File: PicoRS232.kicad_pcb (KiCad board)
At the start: 2 copper layers, 78.7 x 72.9 mm, 25 parts, among them J1 RS232_0, J2 RS232_1, J3 RS232_2, J4 RS232_3, J5 RS232_4, J6 RS232_5, U1 MAX3232CDR, U2 MAX3232CDR, U3 MAX3232CDR

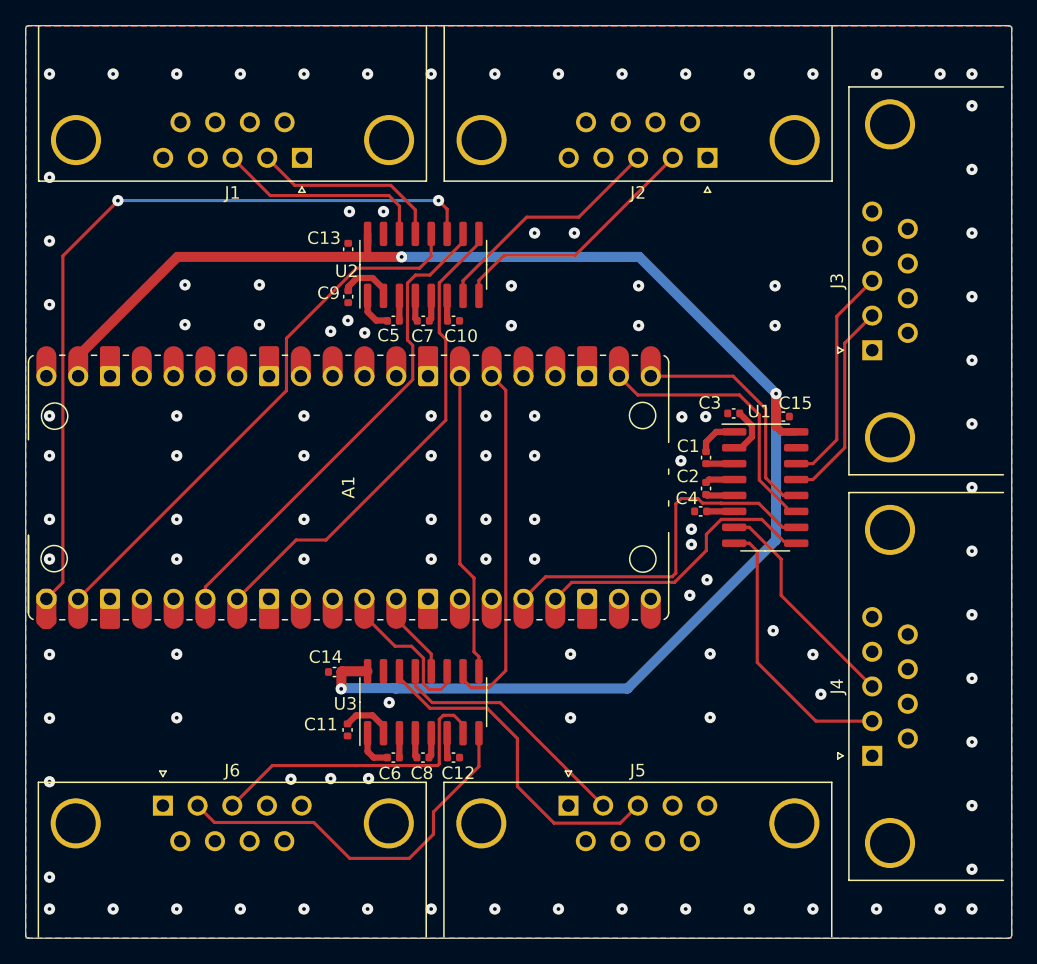
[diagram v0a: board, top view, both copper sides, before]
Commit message: Break out unused GPIO pins to headers.
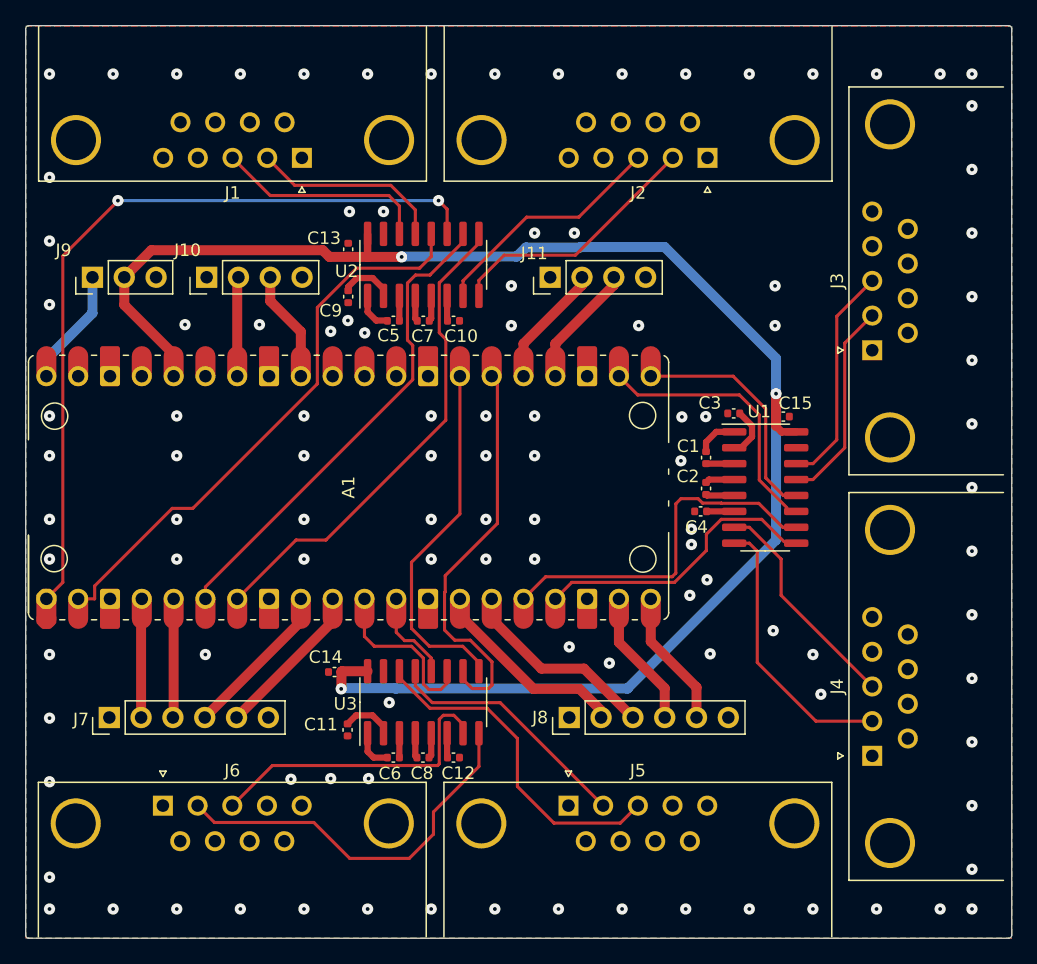
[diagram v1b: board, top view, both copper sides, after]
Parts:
- added J10: Conn_01x04_Male, Connector_PinHeader_2.54mm:PinHeader_1x04_P2.54mm_Vertical, F.Cu at (60.5, 54.5)
- added J11: Conn_01x04_Male, Connector_PinHeader_2.54mm:PinHeader_1x04_P2.54mm_Vertical, F.Cu at (87.9, 54.5)
- added J7: Conn_01x06_Male, Connector_PinHeader_2.54mm:PinHeader_1x06_P2.54mm_Vertical, F.Cu at (52.7, 89.6)
- added J8: Conn_01x06_Male, Connector_PinHeader_2.54mm:PinHeader_1x06_P2.54mm_Vertical, F.Cu at (89.4, 89.6)
- added J9: Conn_01x03_Male, Connector_PinHeader_2.54mm:PinHeader_1x03_P2.54mm_Vertical, F.Cu at (51.3, 54.5)
- J2: value RS232_1 -> RS232_0
- J3: value RS232_2 -> RS232_0
- J4: value RS232_3 -> RS232_0
- J5: value RS232_4 -> RS232_0
- J6: value RS232_5 -> RS232_0
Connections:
- A1 pad 10: unconnected-(A1-Pad10) -> GPIO7
- A1 pad 14: unconnected-(A1-Pad14) -> GPIO10
- A1 pad 15: unconnected-(A1-Pad15) -> GPIO11
- A1 pad 19: unconnected-(A1-Pad19) -> GPIO14
- A1 pad 20: unconnected-(A1-Pad20) -> GPIO15
- A1 pad 24: unconnected-(A1-Pad24) -> GPIO18
- A1 pad 25: unconnected-(A1-Pad25) -> GPIO19
- A1 pad 32: unconnected-(A1-Pad32) -> GPIO27
- A1 pad 34: unconnected-(A1-Pad34) -> GPIO28
- A1 pad 36: unconnected-(A1-Pad36) -> +3V3
- A1 pad 39: +3V3 -> unconnected-(A1-Pad39)
- A1 pad 4: unconnected-(A1-Pad4) -> GPIO2
- A1 pad 5: unconnected-(A1-Pad5) -> GPIO3
- A1 pad 9: unconnected-(A1-Pad9) -> GPIO6
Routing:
- net GPIO10: track 0.00 -> 14.6 mm
- net GPIO11: track 0.00 -> 14.5 mm
- net GPIO6: track 0.00 -> 10.9 mm
- net GPIO7: track 0.00 -> 10.9 mm
- net +5V: track 0.00 -> 9.42 mm
- net GPIO2: track 0.00 -> 9.42 mm
- net GPIO14: track 0.00 -> 9.39 mm
- net GPIO15: track 0.00 -> 9.39 mm
- net GPIO27: track 0.00 -> 8.91 mm
- net GPIO19: track 0.00 -> 8.23 mm
- net GPIO18: track 0.00 -> 8.23 mm
- net GPIO3: track 0.00 -> 7.82 mm
- net GPIO28: track 0.00 -> 7.80 mm
- net +3V3: track 124.6 -> 128.8 mm
- net UART5_RX: track 24.2 -> 28.3 mm
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
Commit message: Organize schematic and add mounting holes.
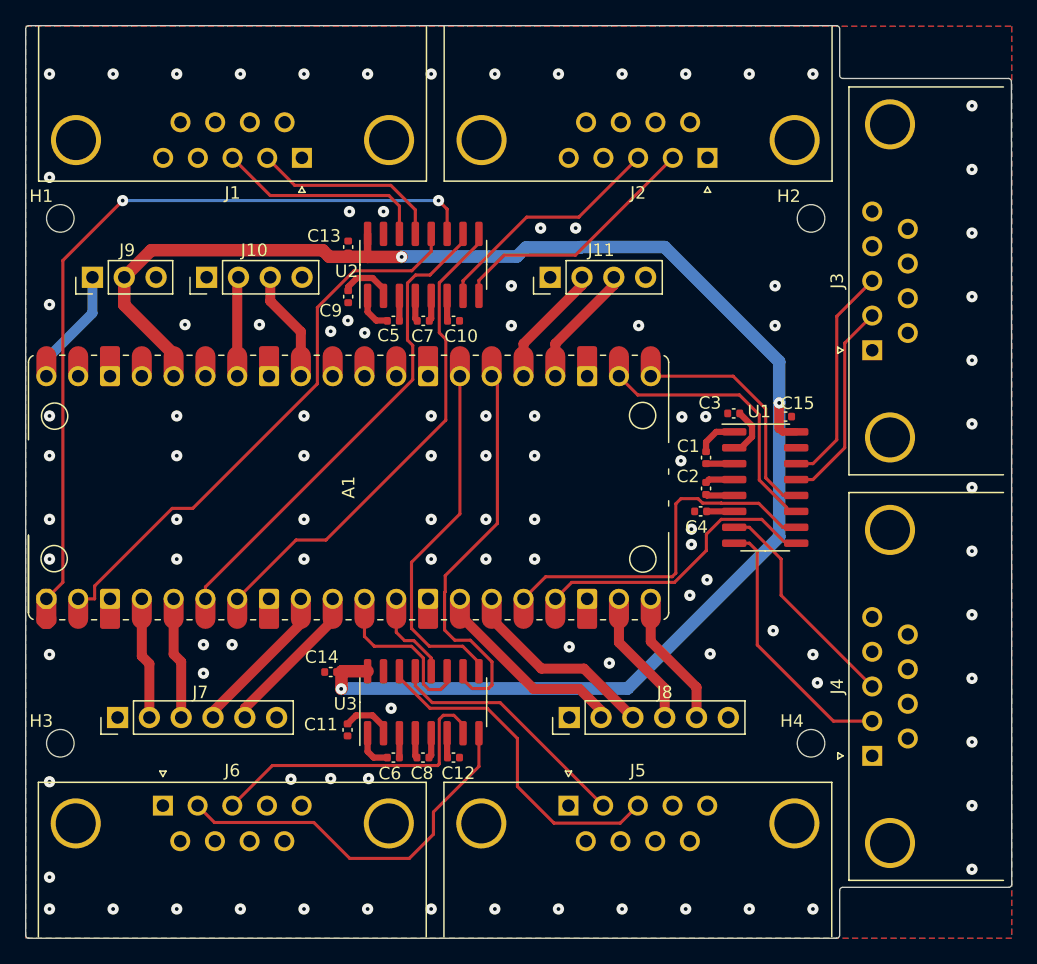
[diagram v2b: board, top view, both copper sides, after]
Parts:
- added H1: MountingHole_2.2mm_M2, MountingHole:MountingHole_2.2mm_M2, F.Cu at (48.8, 49.8)
- added H2: MountingHole_2.2mm_M2, MountingHole:MountingHole_2.2mm_M2, F.Cu at (108.7, 49.8)
- added H3: MountingHole_2.2mm_M2, MountingHole:MountingHole_2.2mm_M2, F.Cu at (48.8, 91.7)
- added H4: MountingHole_2.2mm_M2, MountingHole:MountingHole_2.2mm_M2, F.Cu at (108.7, 91.7)
- moved J7 0.66 mm to (53.3, 89.6)
- moved C14 0.30 mm to (70.4, 86.0)
- moved C15 0.18 mm to (106.7, 65.6)
- moved C13 0.18 mm to (71.8, 52.1)
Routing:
- net GPIO2: track 9.42 -> 8.13 mm
- net RS232_3_RX: track 22.1 -> 21.3 mm
- net +3V3: track 128.8 -> 128.1 mm
- net GND: vias 108 -> 102
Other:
- outline, holes or cut-outs redrawn

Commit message: Silkscreen and cosmetic improvements to PCB.
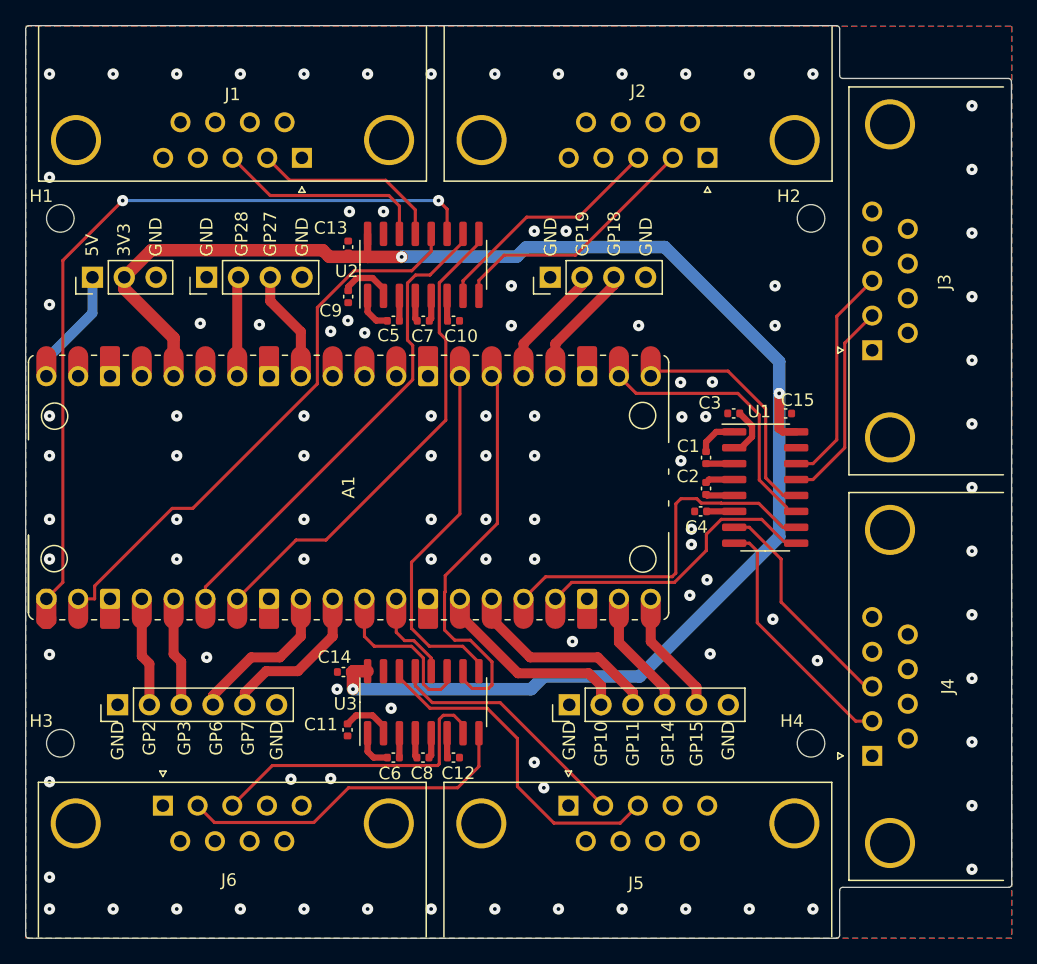
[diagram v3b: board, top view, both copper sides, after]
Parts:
- moved J7 1.02 mm to (53.3, 88.6)
- moved J8 1.02 mm to (89.4, 88.6)
- moved C14 1.02 mm to (71.4, 86.0)
- moved C15 0.25 mm to (106.7, 65.4)
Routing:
- net RS232_5_RX: track 30.9 -> 27.5 mm
- net +3V3: track 128.1 -> 127.1 mm
- net RS232_3_RX: track 21.3 -> 20.3 mm
- net GPIO3: track 8.13 -> 7.11 mm
- net GPIO2: track 8.13 -> 7.11 mm
- net GPIO15: track 9.39 -> 8.37 mm
- net GPIO14: track 9.39 -> 8.37 mm
- net GPIO10: track 14.6 -> 15.2 mm
- net GPIO11: track 14.5 -> 14.0 mm
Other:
- board text added: "3V3"
- board text added: "5V"
- board text added: "GND"
- board text added: "GP10"
- board text added: "GP11"
- board text added: "GP14"
- board text added: "GP15"
- board text added: "GP18"
- board text added: "GP19"
- board text added: "GP2"
- board text added: "GP27"
- board text added: "GP28"
- board text added: "GP3"
- board text added: "GP6"
- board text added: "GP7"

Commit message: Add a reset button and merge two pin headers.
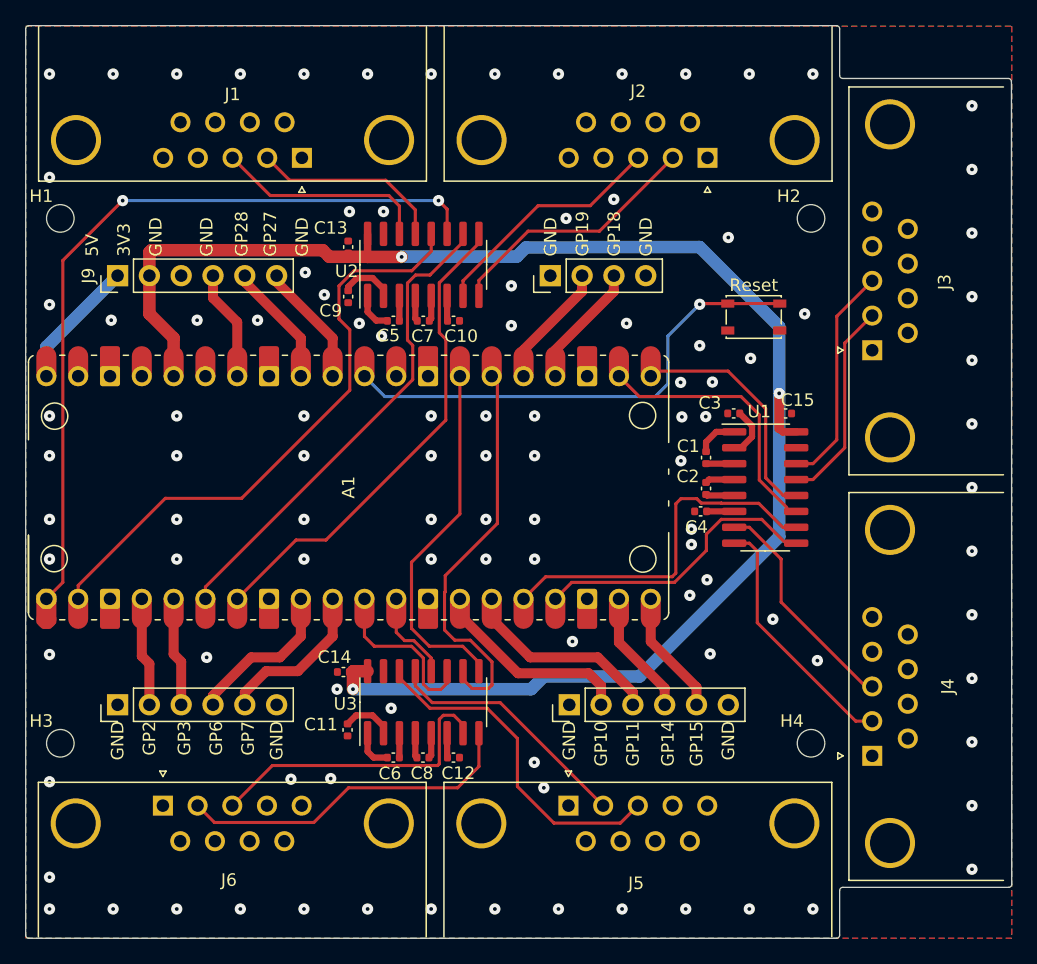
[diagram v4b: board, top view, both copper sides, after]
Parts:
- removed J11: Conn_01x04_Male, Connector_PinHeader_2.54mm:PinHeader_1x04_P2.54mm_Vertical
- added SW1: Reset, Button_Switch_SMD:SW_SPST_PTS810, F.Cu at (104.1, 57.7)
- J9: value Conn_01x03_Male -> Conn_01x06_Male; footprint Connector_PinHeader_2.54mm:PinHeader_1x03_P2.54mm_Vertical -> Connector_PinHeader_2.54mm:PinHeader_1x06_P2.54mm_Vertical
- moved J10 27.4 mm to (87.9, 54.4)
- moved J9 2.01 mm to (53.3, 54.4)
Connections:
- A1 pad 30: unconnected-(A1-Pad30) -> /Reset
- A1 pad 31: unconnected-(A1-Pad31) -> GPIO26
- J10 pad 2: GPIO28 -> GPIO19
- J10 pad 3: GPIO27 -> GPIO18
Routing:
- net /Reset: track 0.00 -> 39.1 mm, vias 0 -> 1
- net GPIO26: track 0.00 -> 8.28 mm
- net UART0_RX: track 44.5 -> 47.1 mm
- net +5V: track 9.42 -> 10.4 mm
- net GPIO27: track 8.91 -> 8.28 mm
- net GPIO28: track 7.80 -> 7.23 mm
- net GND: vias 102 -> 106

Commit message: Change reset button to one JLCPCB has in stock.
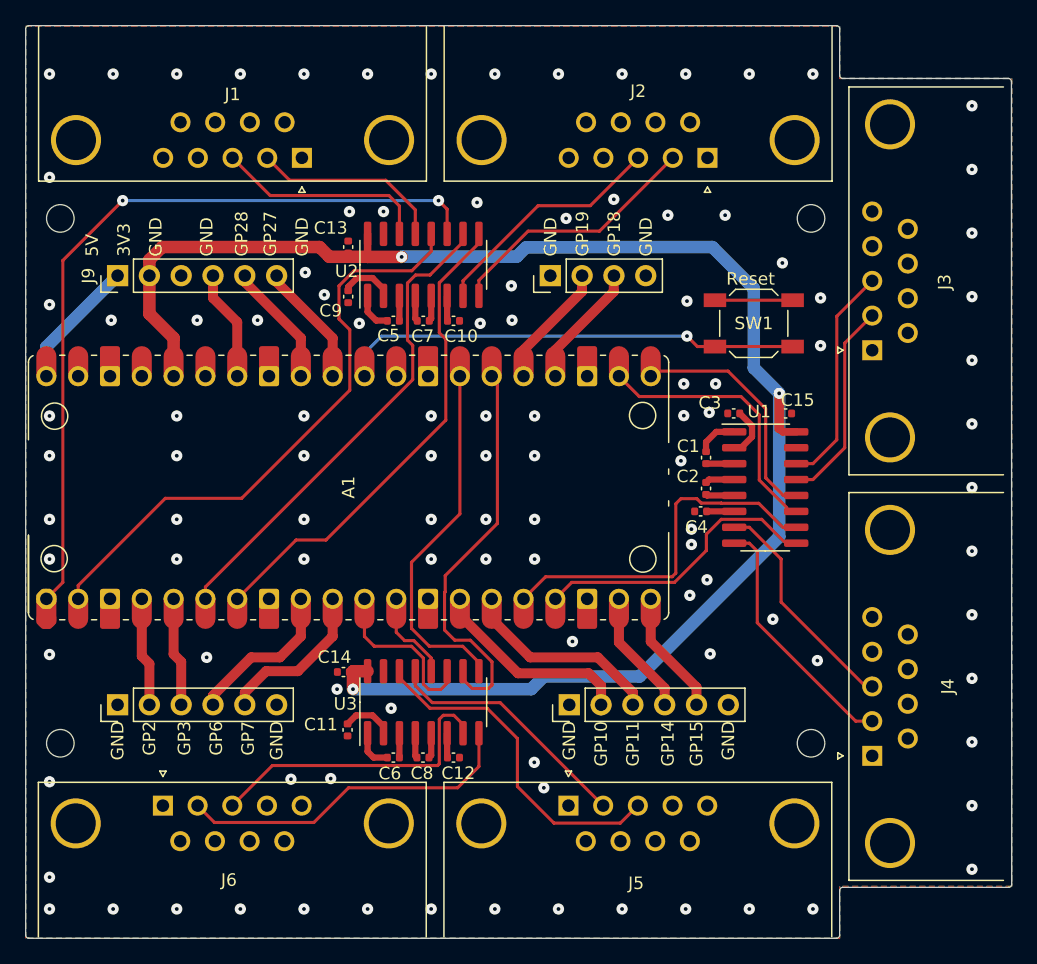
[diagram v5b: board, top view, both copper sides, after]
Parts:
- SW1: footprint Button_Switch_SMD:SW_SPST_PTS810 -> Button_Switch_SMD:SW_SPST_SKQG_WithStem
- moved SW1 0.51 mm to (104.1, 58.2), turned to 180 degrees
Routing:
- net GND: track 0.00 -> 6.20 mm, vias 106 -> 108
- net /Reset: track 39.1 -> 36.9 mm
